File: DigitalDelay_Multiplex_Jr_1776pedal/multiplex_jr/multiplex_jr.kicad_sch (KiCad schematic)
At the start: 68 parts, among them J1 Barrel_Jack, SW3 SW_SPST, U4 VTL5C, U5 L78L05_TO92, U9 PT2399

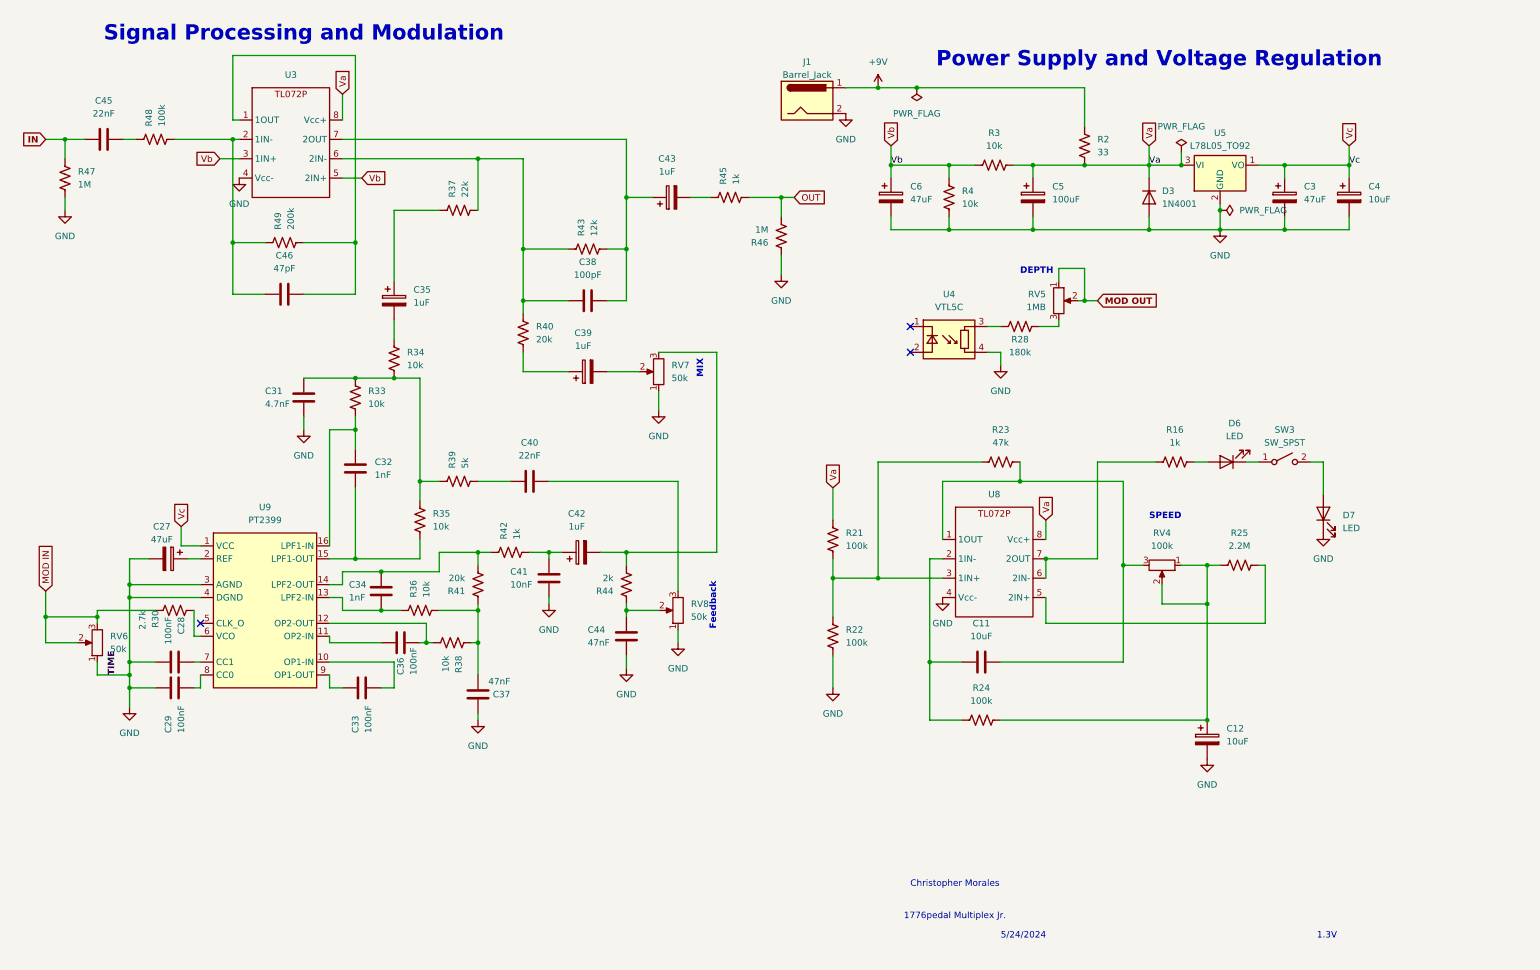
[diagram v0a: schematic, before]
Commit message: Update Multiplex Jr schematic, README, backups, and add footprints/symbols
Co-Authored-By: Claude Opus 5.5 <noreply@anthropic.com>
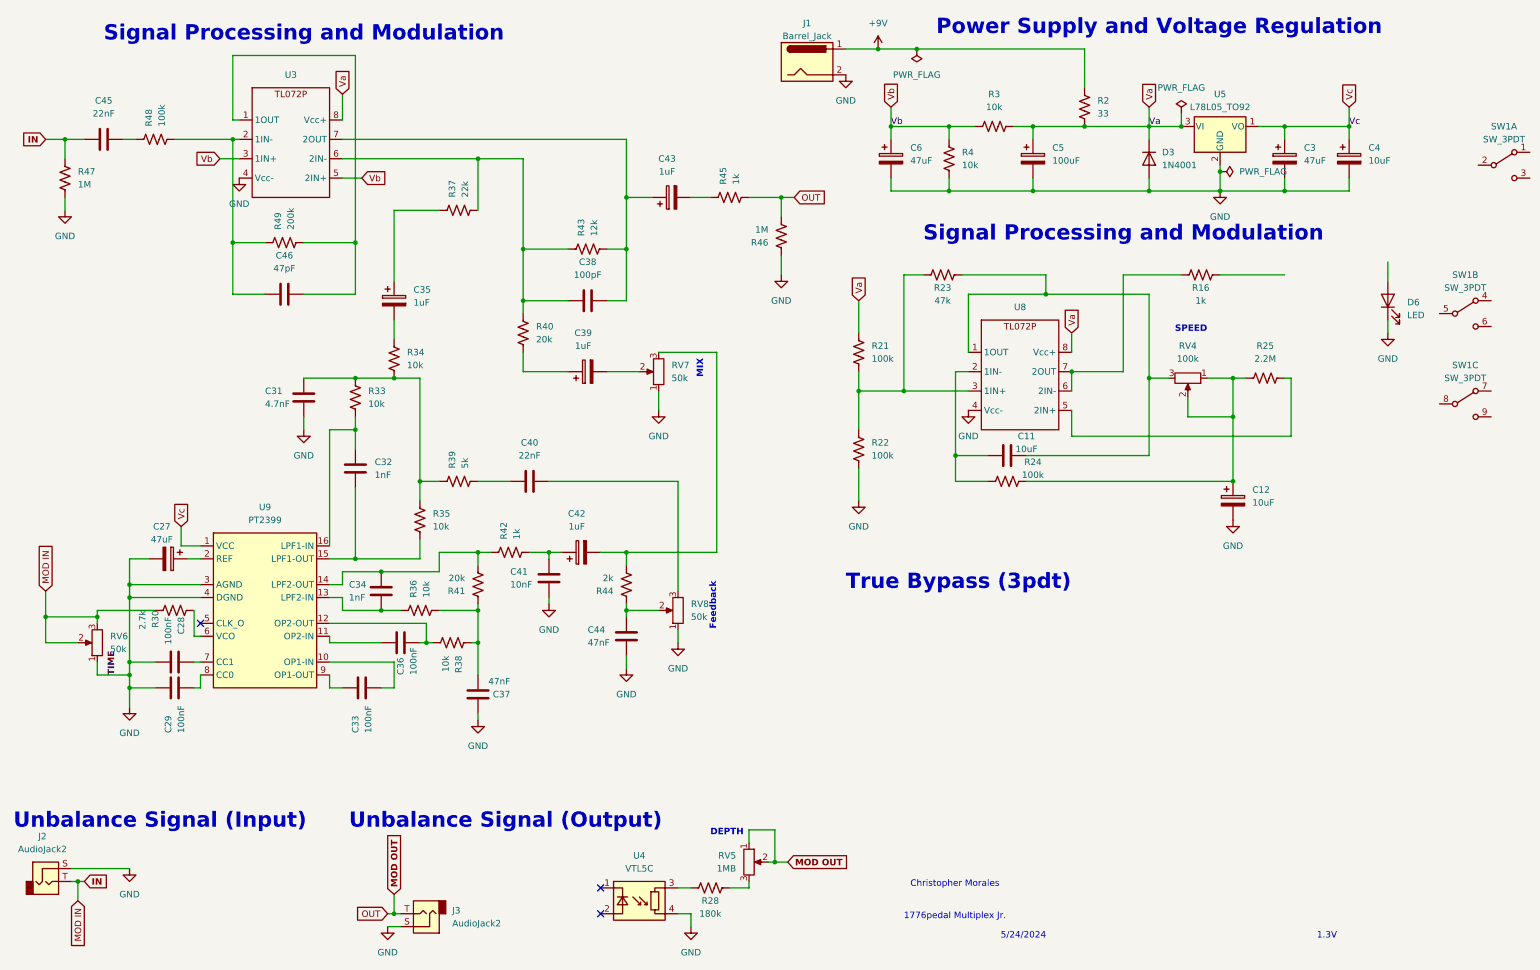
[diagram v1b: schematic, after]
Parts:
- removed D7: LED, LED_THT:LED_D3.0mm, symbol Device:LED
- removed SW3: SW_SPST, symbol Switch:SW_SPST
- added J2, J3: AudioJack2, Connector_Audio:Jack_6.35mm_Neutrik_NMJ4HCD2_Horizontal, symbol Connector_Audio:AudioJack2
- added SW1: SW_3PDT, symbol foot_switch:SW_3PDT
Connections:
- net MOD IN is gone; now on net IN: R30.2, RV6.2, RV6.3
- net OUT is gone; now on net MOD OUT: R45.2, R46.2
- net GND: now also D6.1 (K), J2.S, J3.S
- net IN: now also J2.T
- net MOD OUT: now also J3.T
- net at R23.2, RV4.3, U8.1 (1OUT): now also C11.2; no longer C11.1
- net at R24.1, U8.2 (1IN-): now also C11.1; no longer C11.2
- net at D6.2 (A): no longer R16.2
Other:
- note added: "True Bypass (3pdt)"
- note added: "Unbalance Signal (Input)"
- note added: "Unbalance Signal (Output)"
- moved on the sheet: C11, C12, C3, C4, C5, C6, D3, D6, J1, R16, R2, R21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
